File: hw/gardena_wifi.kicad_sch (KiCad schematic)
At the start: 8 parts, among them J1 RCA, U1 LMZ13608, U2 L298N

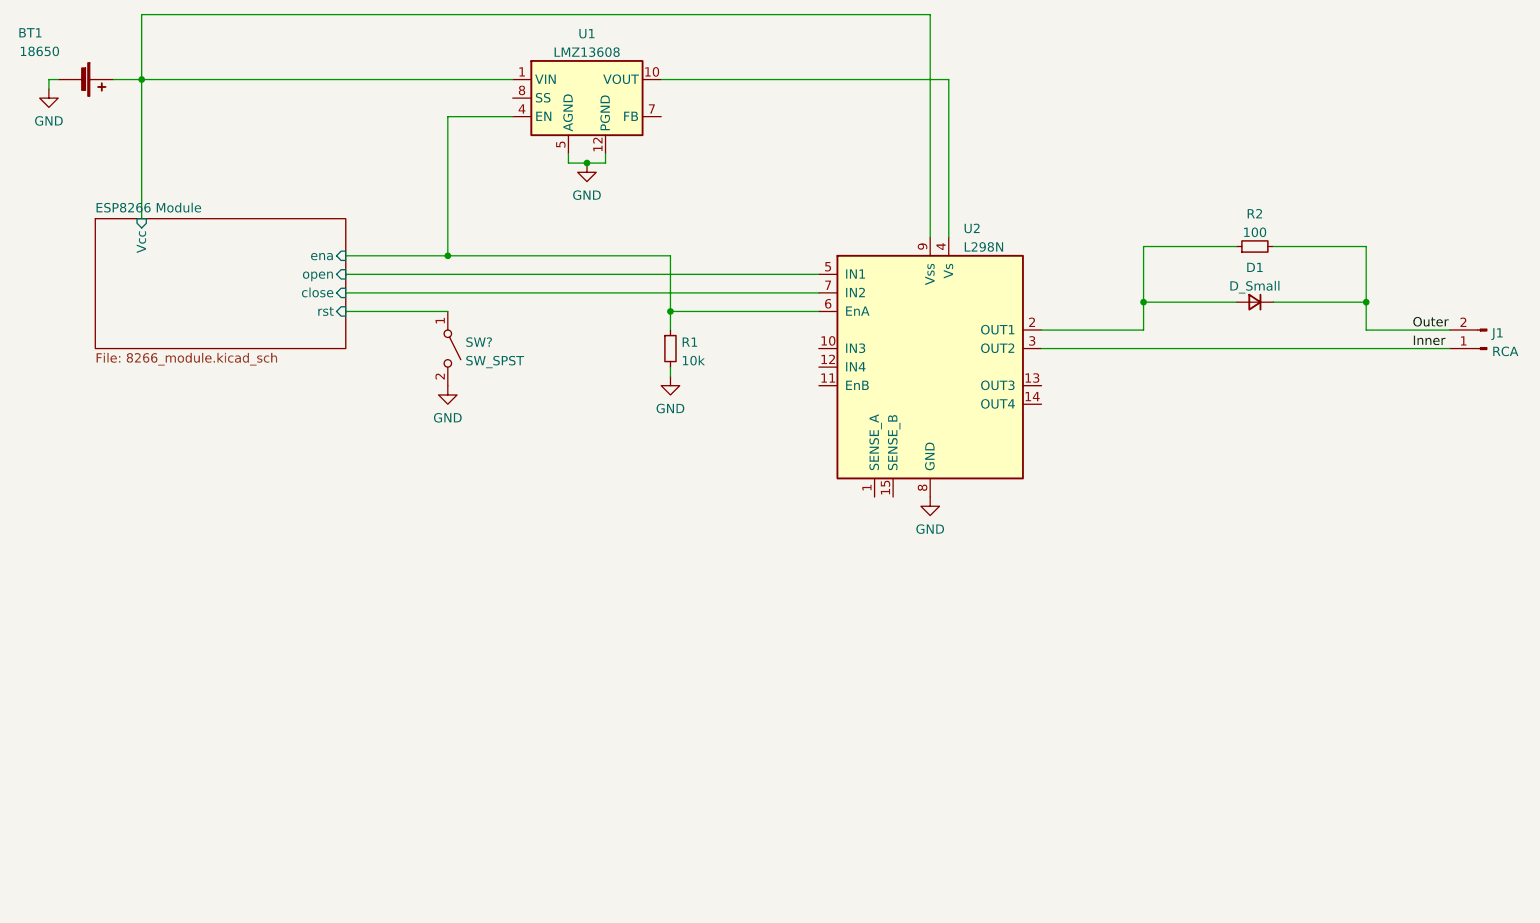
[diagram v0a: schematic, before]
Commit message: Update schematic to include new H bridge
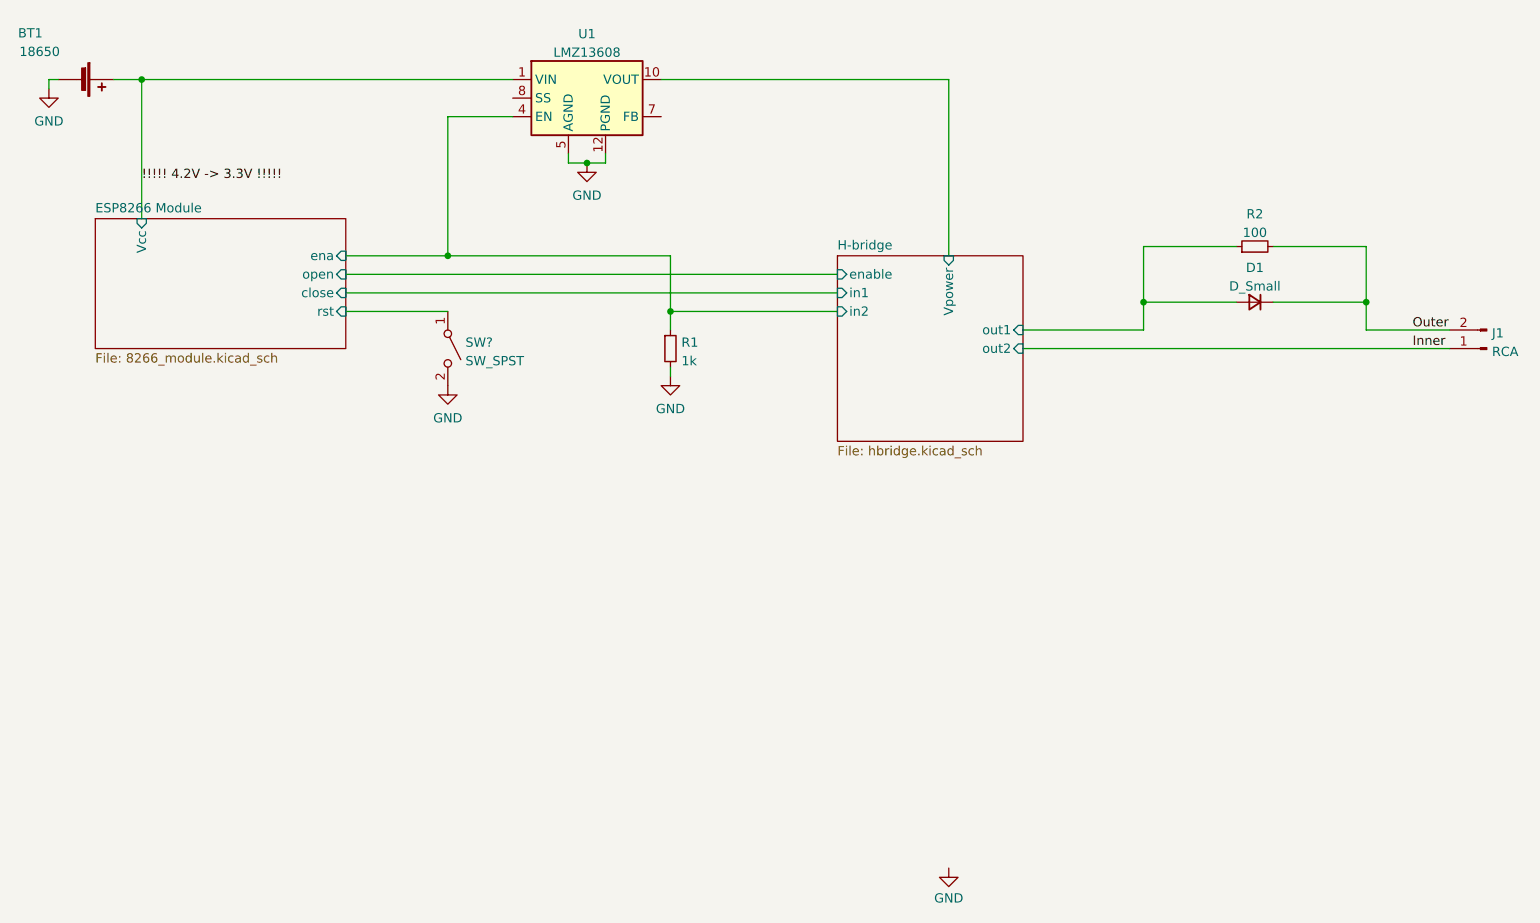
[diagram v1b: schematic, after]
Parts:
- removed U2: L298N, Package_TO_SOT_THT:TO-220-15_P2.54x2.54mm_StaggerOdd_Lead4.58mm_Vertical, symbol Driver_Motor:L298N
- R1: value 10k -> 1k
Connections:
- net H-bridge/out1: now reaches D1.2 (A), R2.1
- net H-bridge/Vpower: now reaches U1.10 (VOUT), U1.11 (VOUT)
- net ESP8266 Module/Vcc renamed !!!!! 4.2V -> 3.3V !!!!!
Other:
- added sheet H-bridge (hbridge.kicad_sch)
